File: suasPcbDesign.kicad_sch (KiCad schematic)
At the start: 36 parts, among them U1 LMR51625DDC, U2 MCP3562RT-E/ST, U3 ESP32-S3-WROOM-1, U4 TLV77733PDBVR, X7R_Cap1 1uF, X7R_Cap2 1uF, X7R_Cap3 1uF, X7R_Cap4 100nF

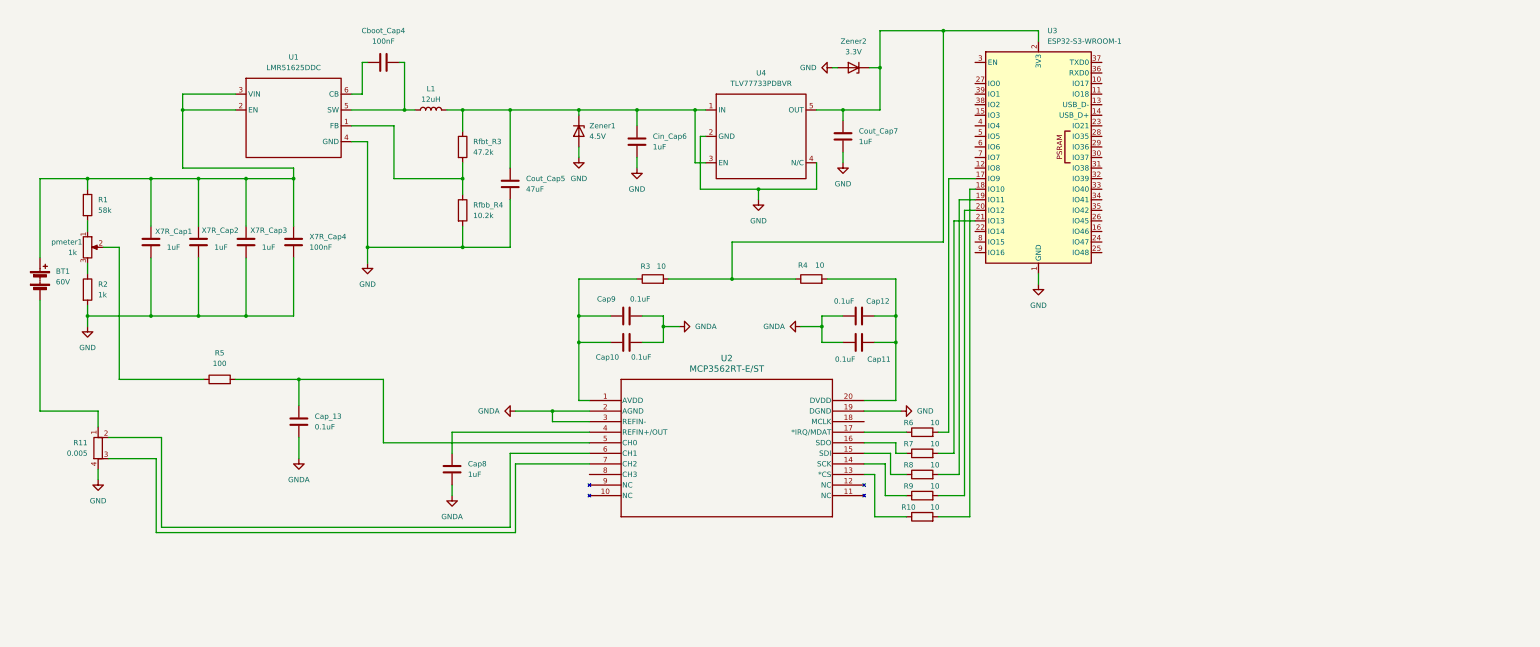
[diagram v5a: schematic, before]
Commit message: added load sensor
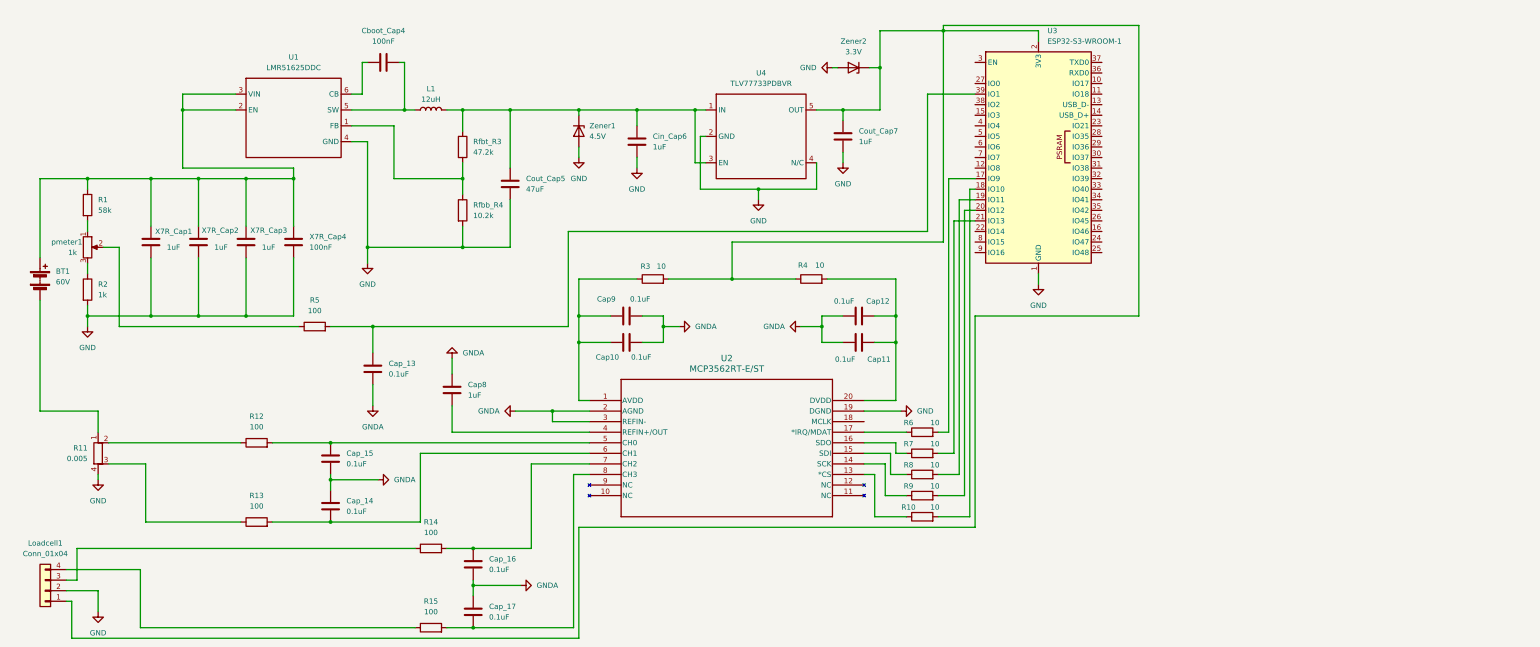
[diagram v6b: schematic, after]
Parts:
- added Cap_14, Cap_15, Cap_16, Cap_17: 0.1uF, symbol Device:C
- added Loadcell1: Conn_01x04, symbol Connector_Generic:Conn_01x04
- added R12, R13, R14, R15: 100, symbol Device:R
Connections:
- net GND: now also Loadcell1.2 (Pin_2)
- net GNDA: now also Cap_14.1, Cap_15.2, Cap_16.2, Cap_17.1
- net at Cap_13.1, R5.2: now also U3.39 (IO1); no longer U2.5 (CH0)
- net at U2.6 (CH1): now also Cap_14.2, R13.2; no longer R11.2
- net at U2.7 (CH2): now also Cap_16.1, R14.2; no longer R11.3
- net at U2.8 (CH3): now also Cap_17.2, R15.2
- net at Cout_Cap7.1, R3.2, R4.1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: now also Loadcell1.1 (Pin_1)
- new net: Cap_15.1, R12.2, U2.5 (CH0)
- new net: Loadcell1.3 (Pin_3), R14.1
- new net: R11.3, R13.1
- new net: R11.2, R12.1
- new net: Loadcell1.4 (Pin_4), R15.1
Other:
- moved on the sheet: Cap8, Cap_13, R11, R5

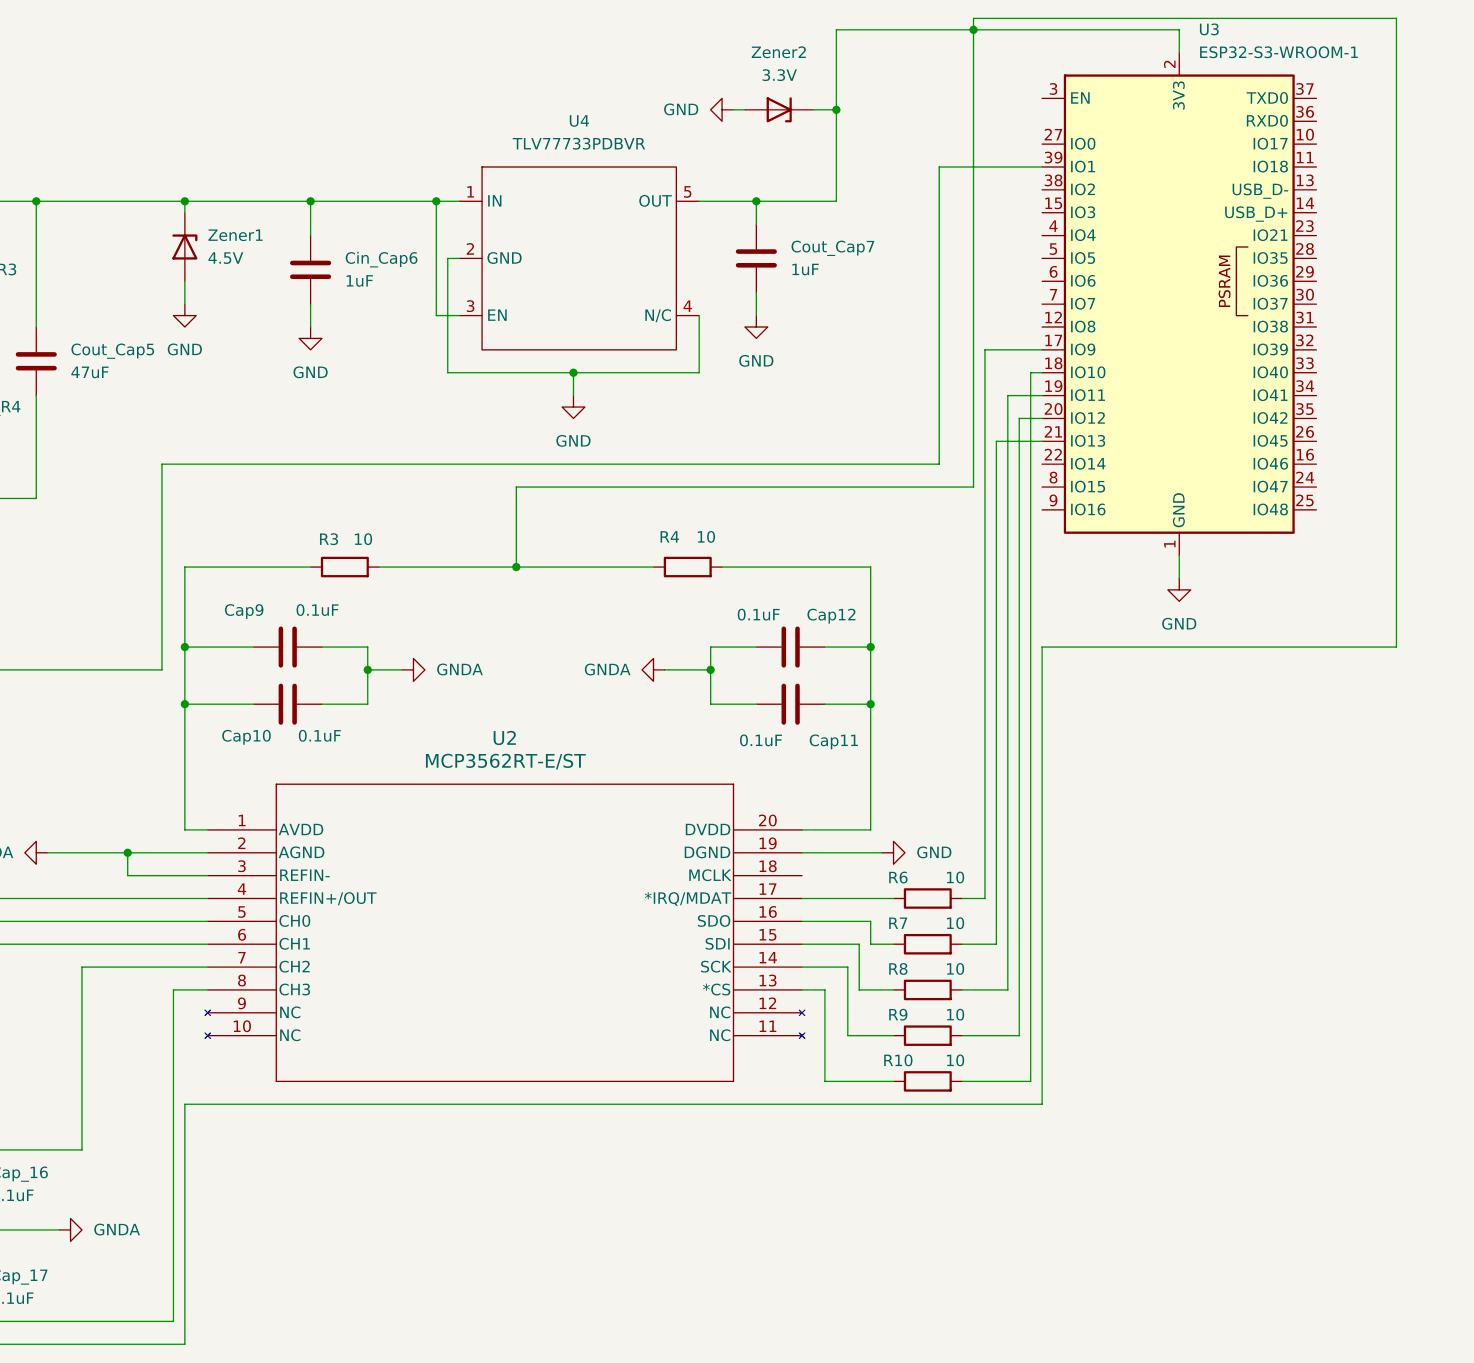
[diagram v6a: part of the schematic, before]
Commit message: added LCD display
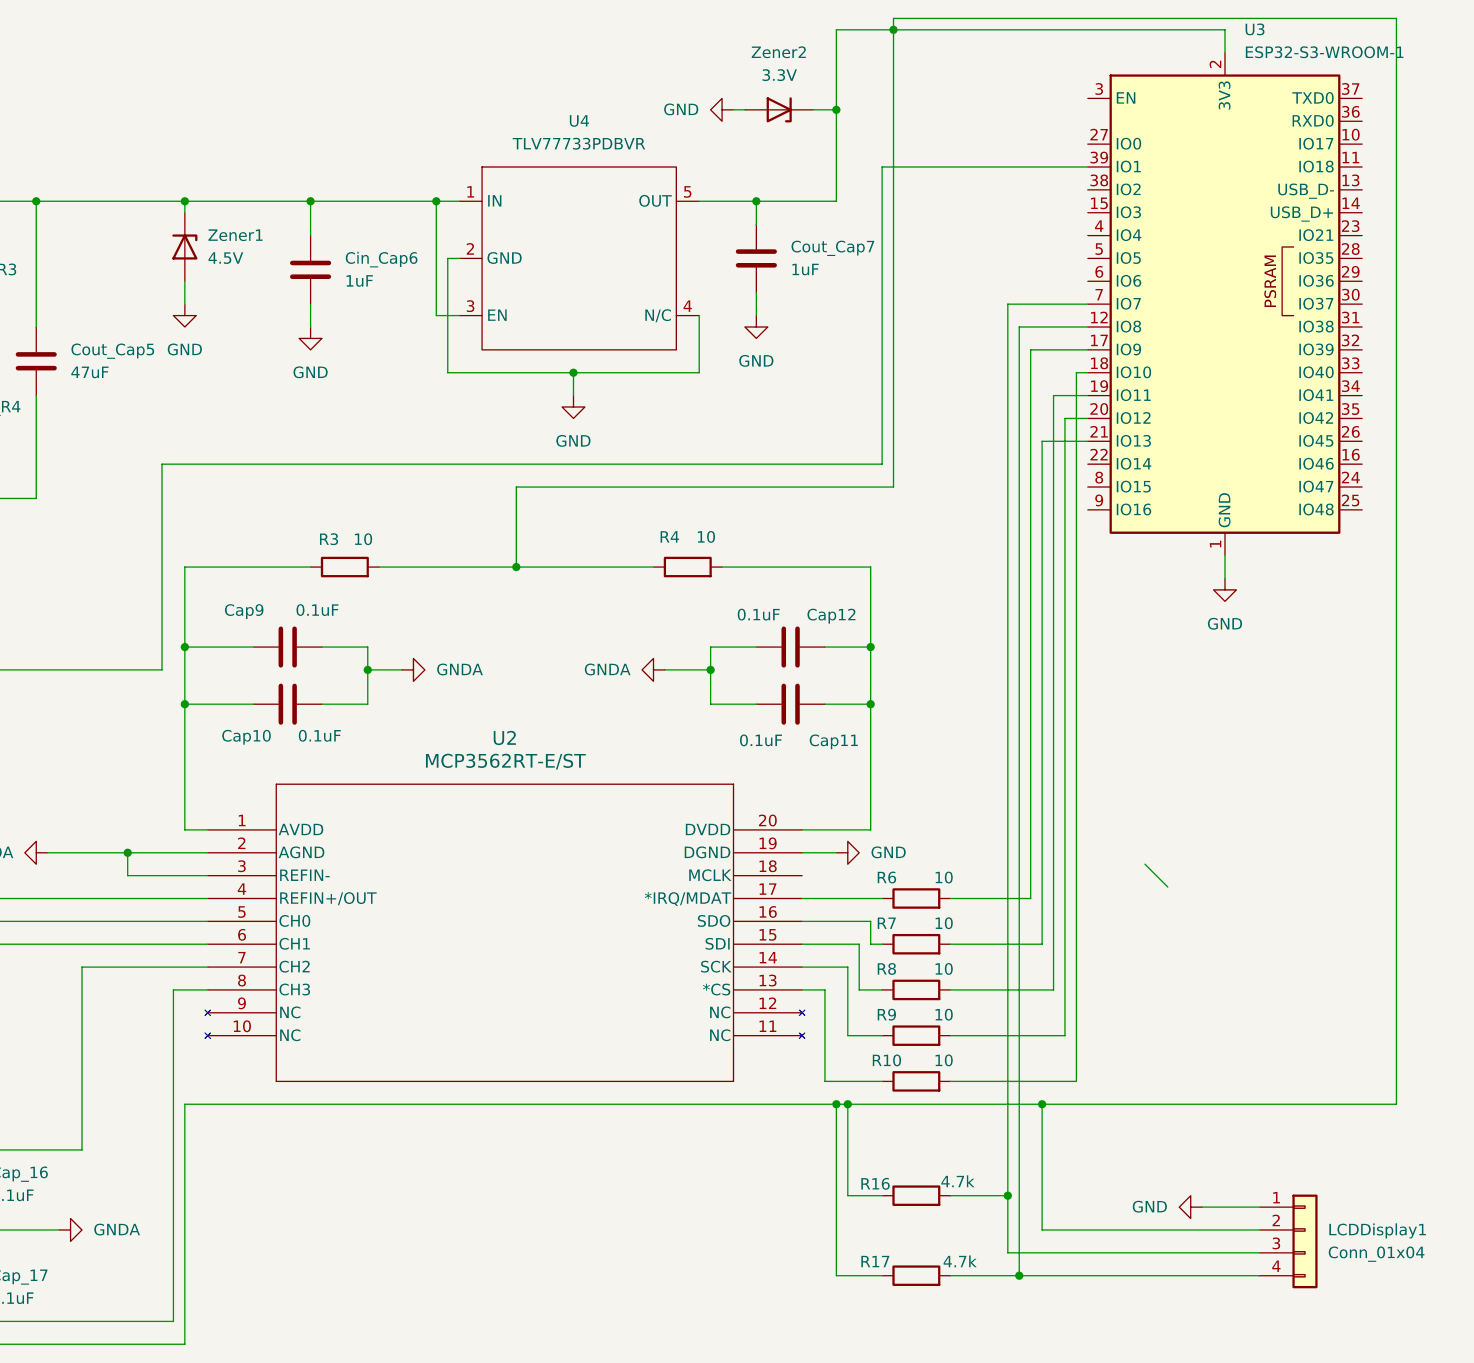
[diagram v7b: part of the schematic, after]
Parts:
- added LCDDisplay1: Conn_01x04, symbol Connector_Generic:Conn_01x04
- added R16, R17: 4.7k, symbol Device:R
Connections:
- net GND: now also LCDDisplay1.1 (Pin_1)
- net at Cout_Cap7.1, Loadcell1.1 (Pin_1), R3.2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: now also LCDDisplay1.2 (Pin_2), R16.1, R17.1
- net at U3.12 (IO8): now also LCDDisplay1.4 (Pin_4), R17.2
- net at U3.7 (IO7): now also LCDDisplay1.3 (Pin_3), R16.2
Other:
- moved on the sheet: R10, R6, R7, R8, R9, U3

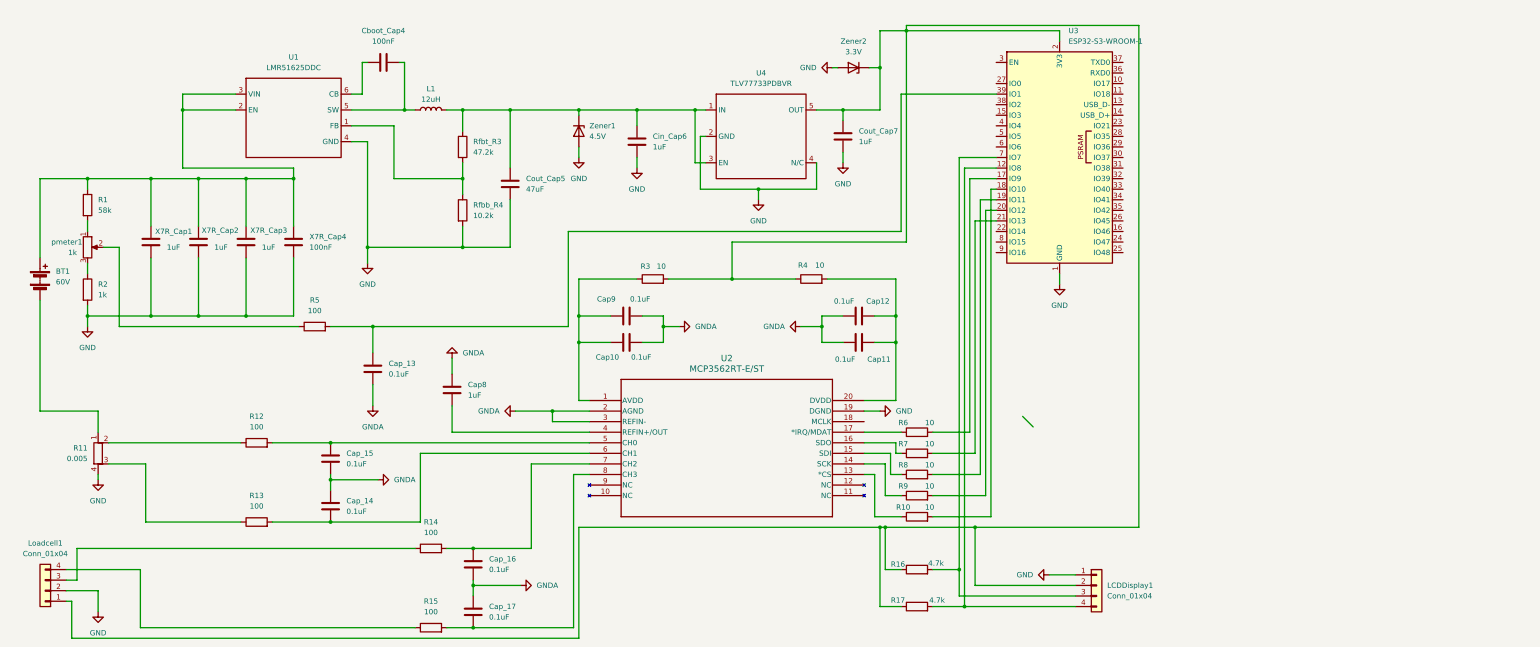
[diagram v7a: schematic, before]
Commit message: added lcd display pins
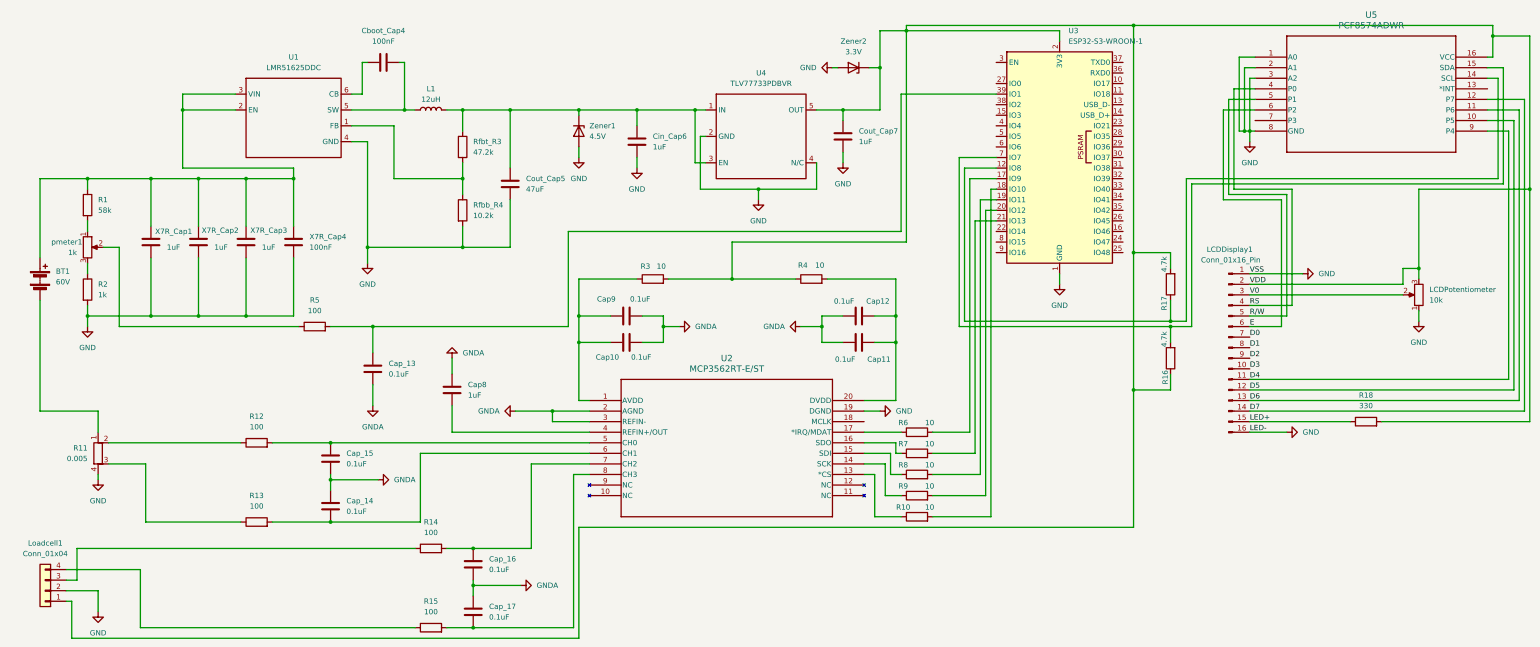
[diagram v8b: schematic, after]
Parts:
- removed LCDDisplay1: Conn_01x04, symbol Connector_Generic:Conn_01x04
- added LCDDisplay1: Conn_01x16_Pin, symbol Connector:Conn_01x16_Pin
- added LCDPotentiometer: 10k, symbol Device:R_Potentiometer
- added R18: 330, symbol Device:R
- added U5: PCF8574ADWR, DW16, symbol suasPcbSymbols:PCF8574ADWR
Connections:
- net GND: now also LCDDisplay1.1 (Pin_1), LCDDisplay1.16 (Pin_16), LCDPotentiometer.1, U5.1 (A0), U5.2 (A1), U5.3 (A2), U5.8 (GND)
- net VDD: now reaches Cout_Cap7.1, Loadcell1.1 (Pin_1), R16.1, R3.2, R4.1, U3.2 (3V3), U4.5 (OUT), Zener2.1 (K)
- net VDD: now also R17.2, LCDDisplay1.2 (Pin_2), LCDPotentiometer.3, R18.2, U5.16 (VCC); no longer R17.1
- net at R16.2, U3.7 (IO7): now also U5.15 (SDA)
- net at U3.12 (IO8): now also R17.1, U5.14 (SCL); no longer R17.2
- new net D0: LCDDisplay1.7 (Pin_7)
- new net D1: LCDDisplay1.8 (Pin_8)
- new net D2: LCDDisplay1.9 (Pin_9)
- new net D3: LCDDisplay1.10 (Pin_10)
- new net D4: LCDDisplay1.11 (Pin_11), U5.9 (P4)
- new net D5: LCDDisplay1.12 (Pin_12), U5.10 (P5)
- new net D6: LCDDisplay1.13 (Pin_13), U5.11 (P6)
- new net D7: LCDDisplay1.14 (Pin_14), U5.12 (P7)
- new net E: LCDDisplay1.6 (Pin_6), U5.6 (P2)
- new net LED+: LCDDisplay1.15 (Pin_15), R18.1
- new net RS: LCDDisplay1.4 (Pin_4), U5.4 (P0)
- new net R/W: LCDDisplay1.5 (Pin_5), U5.5 (P1)
- new net V0: LCDDisplay1.3 (Pin_3), LCDPotentiometer.2
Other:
- moved on the sheet: R16, R17
